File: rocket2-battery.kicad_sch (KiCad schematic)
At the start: 58 parts, among them J1 Conn_01x07, J2 SMA, J3 ARM Cortex Debug, P1 PAD_SMD, P2 PAD_SMD, P3 PAD_SMD, P4 PAD_SMD, P5 PAD_SMD, P6 PAD_SMD, P7 PAD_SMD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

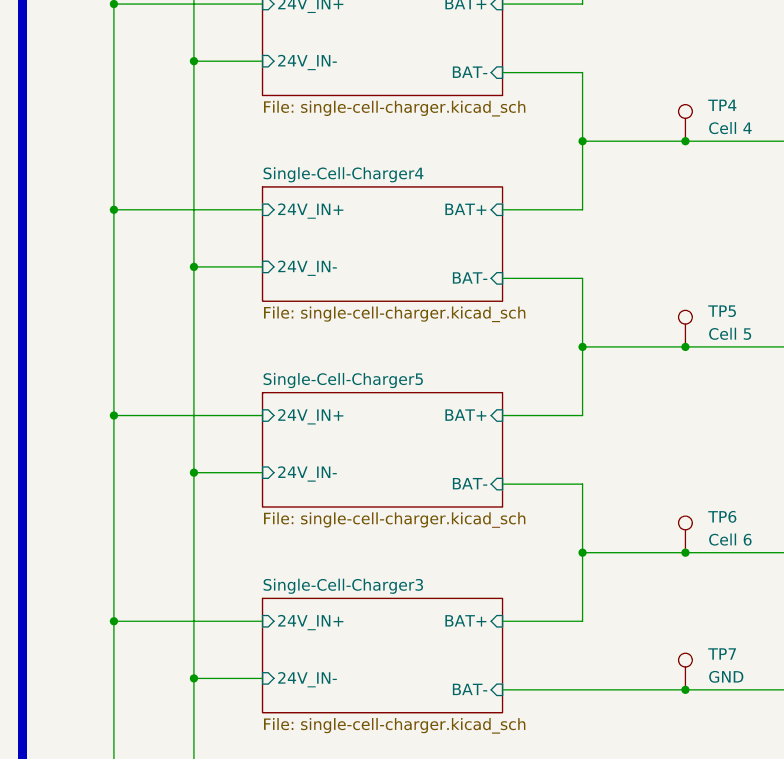
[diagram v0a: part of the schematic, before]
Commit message: Made Charging layout
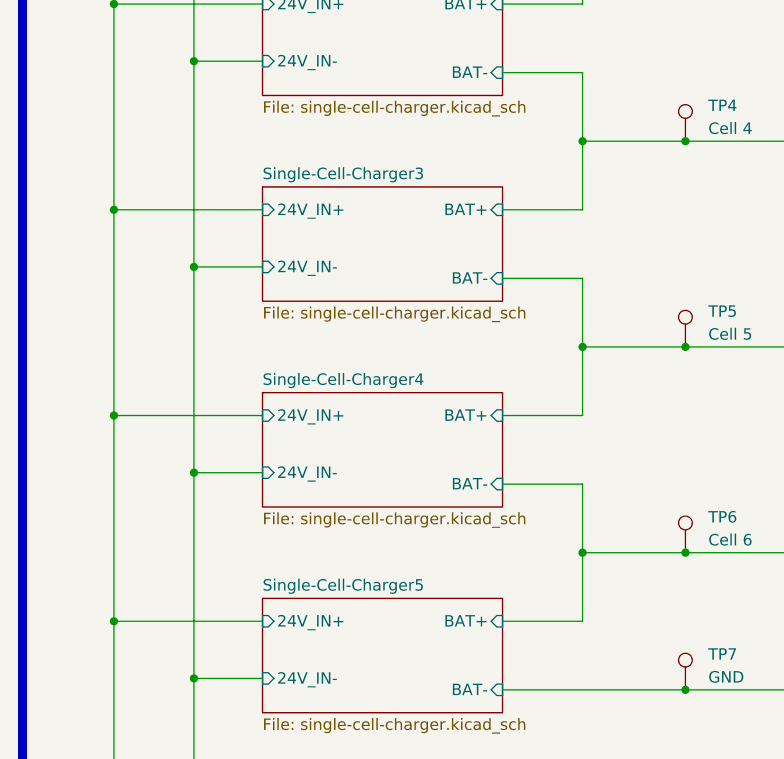
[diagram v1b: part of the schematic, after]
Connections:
- net Single-Cell-Charger3/BAT+ is gone; now on net Single-Cell-Charger4/BAT-: J1.6 (Pin_6), TP6.1
- net Single-Cell-Charger4/BAT-: no longer J1.5 (Pin_5), TP5.1
- new net Single-Cell-Charger3/BAT-: J1.5 (Pin_5), TP5.1
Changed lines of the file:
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@@
     (stroke (width 0.1524) (type solid))
     (fill (color 0 0 0 0.0000))
-    (property "Sheetname" "Single-Cell-Charger3" (at 39.37 142.7984 0)
+    (property "Sheetname" "Single-Cell-Charger5" (at 39.37 142.7984 0)
       (effects (font (size 1.27 1.27)) (justify left bottom))
     )
@@
     (stroke (width 0.1524) (type solid))
     (fill (color 0 0 0 0.0000))
-    (property "Sheetname" "Single-Cell-Charger5" (at 39.37 119.9384 0)
+    (property "Sheetname" "Single-Cell-Charger4" (at 39.37 119.9384 0)
       (effects (font (size 1.27 1.27)) (justify left bottom))
     )
@@
     (stroke (width 0.1524) (type solid))
     (fill (color 0 0 0 0.0000))
-    (property "Sheetname" "Single-Cell-Charger4" (at 39.37 97.0784 0)
+    (property "Sheetname" "Single-Cell-Charger3" (at 39.37 97.0784 0)
       (effects (font (size 1.27 1.27)) (justify left bottom))
     )

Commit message: Squished
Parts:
- U1: value ~ -> 3V3 LDO
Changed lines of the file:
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@@
       (effects (font (size 1.27 1.27)))
     )
-    (property "Value" "~" (at 157.47 161.29 0)
+    (property "Value" "3V3 LDO" (at 157.47 161.29 0)
       (effects (font (size 1.27 1.27)))
     )

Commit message: Almost done routing
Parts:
- removed P4: PAD_SMD, TestPoint:TestPoint_Pad_2.0x2.0mm, symbol pkl_misc:PAD_SMD
- R8: footprint Resistor_SMD:R_0603_1608Metric -> Resistor_SMD:R_0603_1608Metric_Pad0.98x0.95mm_HandSolder
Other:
- moved on the sheet: P7
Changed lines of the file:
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@@
     (stroke (width 0) (type default))
   )
-  (wire (pts (xy 189.23 142.24) (xy 200.66 142.24))
+  (wire (pts (xy 187.96 142.24) (xy 199.39 142.24))
     (stroke (width 0) (type default))
   )
@@
     (stroke (width 0) (type default))
   )
-  (wire (pts (xy 69.85 185.42) (xy 73.66 185.42))
-    (stroke (width 0) (type default))
-  )
   (wire (pts (xy 255.27 95.25) (xy 257.81 95.25))
     (stroke (width 0) (type default))
@@
     (stroke (width 0) (type default))
   )
+  (wire (pts (xy 190.5 137.16) (xy 199.39 137.16))
+    (stroke (width 0) (type default))
+  )
   (wire (pts (xy 147.32 191.77) (xy 152.4 191.77))
     (stroke (width 0) (type default))
@@
     (stroke (width 0) (type default))
   )
-  (wire (pts (xy 69.85 191.77) (xy 73.66 191.77))
-    (stroke (width 0) (type default))
-  )
   (wire (pts (xy 208.28 156.21) (xy 213.36 156.21))
     (stroke (width 0) (type default))
@@
     (effects (font (size 1.27 1.27)) (justify left bottom))
   )
-  (label "MAIN+" (at 189.23 142.24 0) (fields_autoplaced)
+  (label "MAIN+" (at 187.96 142.24 0) (fields_autoplaced)
     (effects (font (size 1.27 1.27)) (justify left bottom))
   )
@@
     (effects (font (size 1.27 1.27)) (justify right bottom))
   )
-  (label "BAT_OUT-" (at 69.85 185.42 180) (fields_autoplaced)
-    (effects (font (size 1.27 1.27)) (justify right bottom))
-  )
   (label "BATT_MAIN+" (at 237.49 109.22 0) (fields_autoplaced)
     (effects (font (size 1.27 1.27)) (justify left bottom))
   )
-  (label "BAT_OUT+" (at 69.85 191.77 180) (fields_autoplaced)
-    (effects (font (size 1.27 1.27)) (justify right bottom))
-  )
   (label "BATT_MAIN+" (at 135.89 158.75 0) (fields_autoplaced)
     (effects (font (size 1.27 1.27)) (justify left bottom))
@@
     )
   )
+  (symbol (lib_id "power:GND") (at 190.5 137.16 270) (unit 1)
+    (in_bom yes) (on_board yes) (dnp no)
+    (property "Reference" "#PWR044" (at 184.15 137.16 0)
+      (effects (font (size 1.27 1.27)) hide)
+    )
+    (property "Value" "GND" (at 194.31 135.89 90)
+      (effects (font (size 1.27 1.27)) (justify right))
+    )
+    (property "Footprint" "" (at 190.5 137.16 0)
+      (effects (font (size 1.27 1.27)) hide)
+    )
+    (property "Datasheet" "" (at 190.5 137.16 0)
+      (effects (font (size 1.27 1.27)) hide)
+    )
+    (pin "1")
+    (instances
+      (project "rocket2-battery"
+        (path "/453543af-7e3c-49a0-a644-4bd49c4f86f8"
+          (reference "#PWR044") (unit 1)
+        )
+      )
+    )
+  )
   (symbol (lib_id "Device:LED_Small") (at 222.25 62.23 180) (unit 1)
     (in_bom yes) (on_board yes) (dnp no)
@@
     )
   )
-  (symbol (lib_id "pkl_misc:PAD_SMD") (at 78.74 191.77 0) (unit 1)
-    (in_bom yes) (on_board yes) (dnp no) (fields_autoplaced)
-    (property "Reference" "P4" (at 81.28 191.135 0)
-      (effects (font (size 1.524 1.524)) (justify left))
-    )
-    (property "Value" "PAD_SMD" (at 81.28 193.675 0)
-      (effects (font (size 1.524 1.524)) (justify left))
-    )
-    (property "Footprint" "TestPoint:TestPoint_Pad_2.0x2.0mm" (at 78.74 198.12 0)
-      (effects (font (size 1.524 1.524)) hide)
-    )
-    (property "Datasheet" "~" (at 78.74 195.58 0)
-      (effects (font (size 1.524 1.524)))
-    )
-    (property "Manufacturer" "Generic" (at 78.74 191.77 0)
-      (effects (font (size 1.27 1.27)) hide)
-    )
-    (pin "1")
-    (instances
-      (project "rocket2-battery"
-        (path "/453543af-7e3c-49a0-a644-4bd49c4f86f8"
-          (reference "P4") (unit 1)
-        )
-      )
-    )
-  )
   (symbol (lib_id "Device:C_Small") (at 210.82 22.86 0) (unit 1)
     (in_bom yes) (on_board yes) (dnp no)
@@
     )
   )
-  (symbol (lib_id "pkl_misc:PAD_SMD") (at 78.74 185.42 0) (unit 1)
-    (in_bom yes) (on_board yes) (dnp no) (fields_autoplaced)
-    (property "Reference" "P3" (at 81.28 184.785 0)
-      (effects (font (size 1.524 1.524)) (justify left))
-    )
-    (property "Value" "PAD_SMD" (at 81.28 187.325 0)
-      (effects (font (size 1.524 1.524)) (justify left))
-    )
-    (property "Footprint" "TestPoint:TestPoint_Pad_2.0x2.0mm" (at 78.74 191.77 0)
-      (effects (font (size 1.524 1.524)) hide)
-    )
-    (property "Datasheet" "~" (at 78.74 189.23 0)
-      (effects (font (size 1.524 1.524)))
-    )
-    (property "Manufacturer" "Generic" (at 78.74 185.42 0)
-      (effects (font (size 1.27 1.27)) hide)
-    )
-    (pin "1")
-    (instances
-      (project "rocket2-battery"
-        (path "/453543af-7e3c-49a0-a644-4bd49c4f86f8"
-          (reference "P3") (unit 1)
-        )
-      )
-    )
-  )
   (symbol (lib_id "power:+3.3V") (at 275.59 58.42 0) (unit 1)
     (in_bom yes) (on_board yes) (dnp no)
@@
     )
   )
+  (symbol (lib_id "pkl_misc:PAD_SMD") (at 204.47 137.16 0) (unit 1)
+    (in_bom yes) (on_board yes) (dnp no) (fields_autoplaced)
+    (property "Reference" "P3" (at 207.01 136.525 0)
+      (effects (font (size 1.524 1.524)) (justify left))
+    )
+    (property "Value" "PAD_SMD" (at 207.01 139.065 0)
+      (effects (font (size 1.524 1.524)) (justify left))
+    )
+    (property "Footprint" "TestPoint:TestPoint_Pad_2.0x2.0mm" (at 204.47 143.51 0)
+      (effects (font (size 1.524 1.524)) hide)
+    )
+    (property "Datasheet" "~" (at 204.47 140.97 0)
+      (effects (font (size 1.524 1.524)))
+    )
+    (property "Manufacturer" "Generic" (at 204.47 137.16 0)
+      (effects (font (size 1.27 1.27)) hide)
+    )
+    (pin "1")
+    (instances
+      (project "rocket2-battery"
+        (path "/453543af-7e3c-49a0-a644-4bd49c4f86f8"
+          (reference "P3") (unit 1)
+        )
+      )
+    )
+  )
   (symbol (lib_id "Connector:Conn_Coaxial") (at 232.41 93.98 90) (mirror x) (unit 1)
     (in_bom yes) (on_board yes) (dnp no)
@@
     )
   )
-  (symbol (lib_id "pkl_misc:PAD_SMD") (at 205.74 142.24 0) (unit 1)
+  (symbol (lib_id "pkl_misc:PAD_SMD") (at 204.47 142.24 0) (unit 1)
     (in_bom yes) (on_board yes) (dnp no) (fields_autoplaced)
-    (property "Reference" "P7" (at 208.28 141.605 0)
+    (property "Reference" "P7" (at 207.01 141.605 0)
       (effects (font (size 1.524 1.524)) (justify left))
     )
-    (property "Value" "PAD_SMD" (at 208.28 144.145 0)
+    (property "Value" "PAD_SMD" (at 207.01 144.145 0)
       (effects (font (size 1.524 1.524)) (justify left))
     )
-    (property "Footprint" "TestPoint:TestPoint_Pad_2.0x2.0mm" (at 205.74 148.59 0)
+    (property "Footprint" "TestPoint:TestPoint_Pad_2.0x2.0mm" (at 204.47 148.59 0)
       (effects (font (size 1.524 1.524)) hide)
     )
-    (property "Datasheet" "~" (at 205.74 146.05 0)
+    (property "Datasheet" "~" (at 204.47 146.05 0)
       (effects (font (size 1.524 1.524)))
     )
-    (property "Manufacturer" "Generic" (at 205.74 142.24 0)
+    (property "Manufacturer" "Generic" (at 204.47 142.24 0)
       (effects (font (size 1.27 1.27)) hide)
     )
@@
       (effects (font (size 1.27 1.27)))
     )
-    (property "Footprint" "Resistor_SMD:R_0603_1608Metric" (at 213.36 62.23 0)
+    (property "Footprint" "Resistor_SMD:R_0603_1608Metric_Pad0.98x0.95mm_HandSolder" (at 213.36 62.23 0)
       (effects (font (size 1.27 1.27)) hide)
     )

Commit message: Finished most of layout
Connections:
- net MOSFET1: now also U2.11 (PA1); no longer U2.10 (PA0)
- net MOSFET2: now also U2.12 (PA2); no longer U2.11 (PA1)
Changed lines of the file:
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@@
   (no_connect (at 160.02 83.82))
   (no_connect (at 160.02 72.39))
-  (no_connect (at 160.02 46.99))
+  (no_connect (at 160.02 41.91))
   (no_connect (at 160.02 88.9))
   (no_connect (at 160.02 62.23))
@@
     )
   )
-  (global_label "MOSFET1" (shape input) (at 160.02 41.91 180) (fields_autoplaced)
-    (effects (font (size 1.27 1.27)) (justify right))
-    (property "Intersheetrefs" "${INTERSHEET_REFS}" (at 148.7081 41.91 0)
+  (global_label "MOSFET1" (shape input) (at 160.02 44.45 180) (fields_autoplaced)
+    (effects (font (size 1.27 1.27)) (justify right))
+    (property "Intersheetrefs" "${INTERSHEET_REFS}" (at 148.7081 44.45 0)
       (effects (font (size 1.27 1.27)) (justify right) hide)
     )
@@
     )
   )
-  (global_label "MOSFET2" (shape input) (at 160.02 44.45 180) (fields_autoplaced)
-    (effects (font (size 1.27 1.27)) (justify right))
-    (property "Intersheetrefs" "${INTERSHEET_REFS}" (at 148.7081 44.45 0)
-      (effects (font (size 1.27 1.27)) (justify right) hide)
-    )
+  (global_label "MOSFET2" (shape input) (at 160.02 46.99 180) (fields_autoplaced)
+    (effects (font (size 1.27 1.27)) (justify right))
+    (property "Intersheetrefs" "${INTERSHEET_REFS}" (at 148.7081 46.99 0)
+      (effects (font (size 1.27 1.27)) (justify right) hide)
+    )

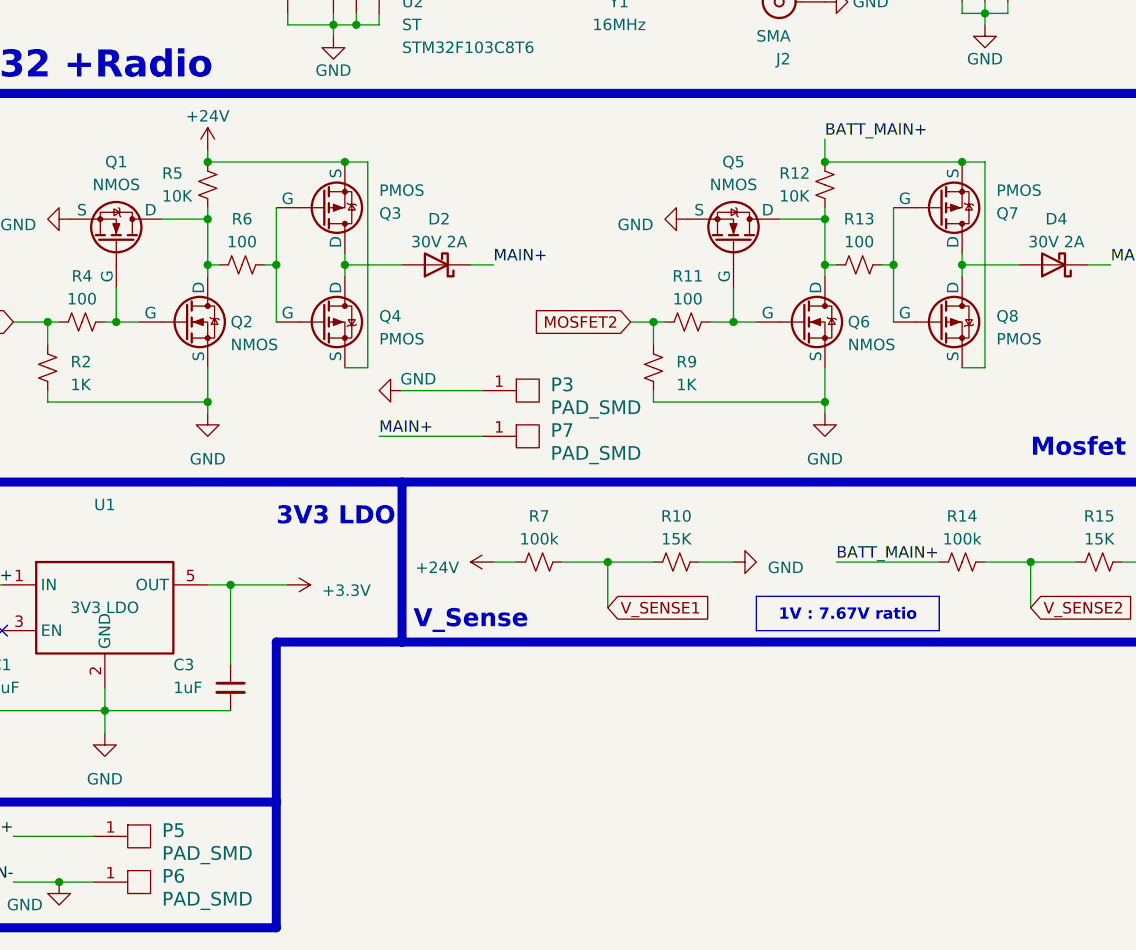
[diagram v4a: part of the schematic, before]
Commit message: Changed PMOS
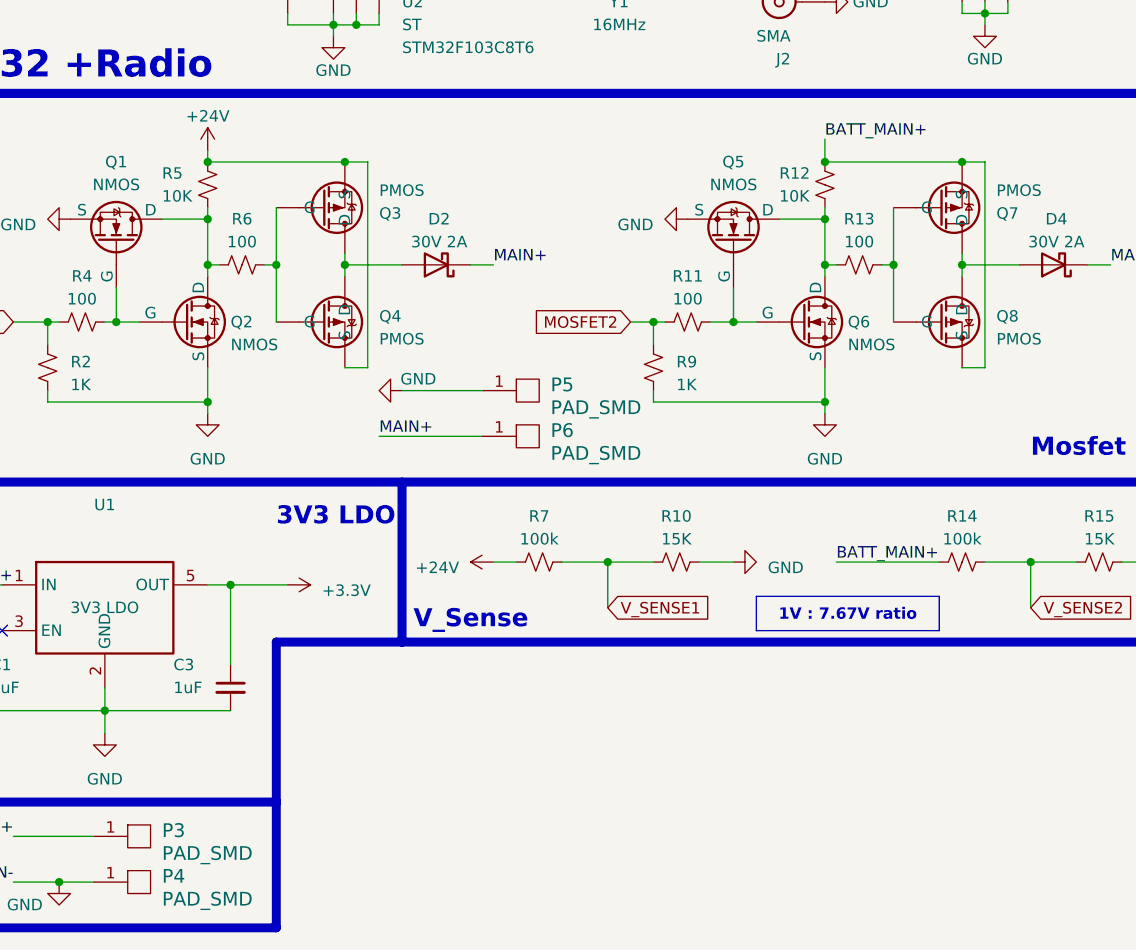
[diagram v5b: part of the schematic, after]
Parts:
- removed Q3, Q4, Q7, Q8: PMOS, Package_TO_SOT_SMD:SOT-23-3, symbol Simulation_SPICE:PMOS
- added Q3, Q4, Q7, Q8: PMOS, Package_SO:Vishay_PowerPAK_1212-8_Single, symbol Transistor_FET:SiSS27DN
- renumbered P5 to P3, P6 to P4, P3 to P5, P7 to P6
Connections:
- net +24V: now also Q3.1 (S), Q3.2 (S), Q3.3 (S), Q4.1 (S), Q4.2 (S), Q4.3 (S)
- net BATT_MAIN+: now also Q7.1 (S), Q7.2 (S), Q7.3 (S), Q8.1 (S), Q8.2 (S), Q8.3 (S)
- net at R6.2: now also Q3.4 (G), Q4.4 (G)
- net at D2.2 (A): now also Q3.5 (D), Q4.5 (D)
- net at R13.2: now also Q7.4 (G), Q8.4 (G)
- net at D4.2 (A): now also Q7.5 (D), Q8.5 (D)
